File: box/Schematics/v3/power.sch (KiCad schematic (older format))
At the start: 29 parts, among them U1 AMC1100DWV, U3 ISL21010CFH333Z-TK

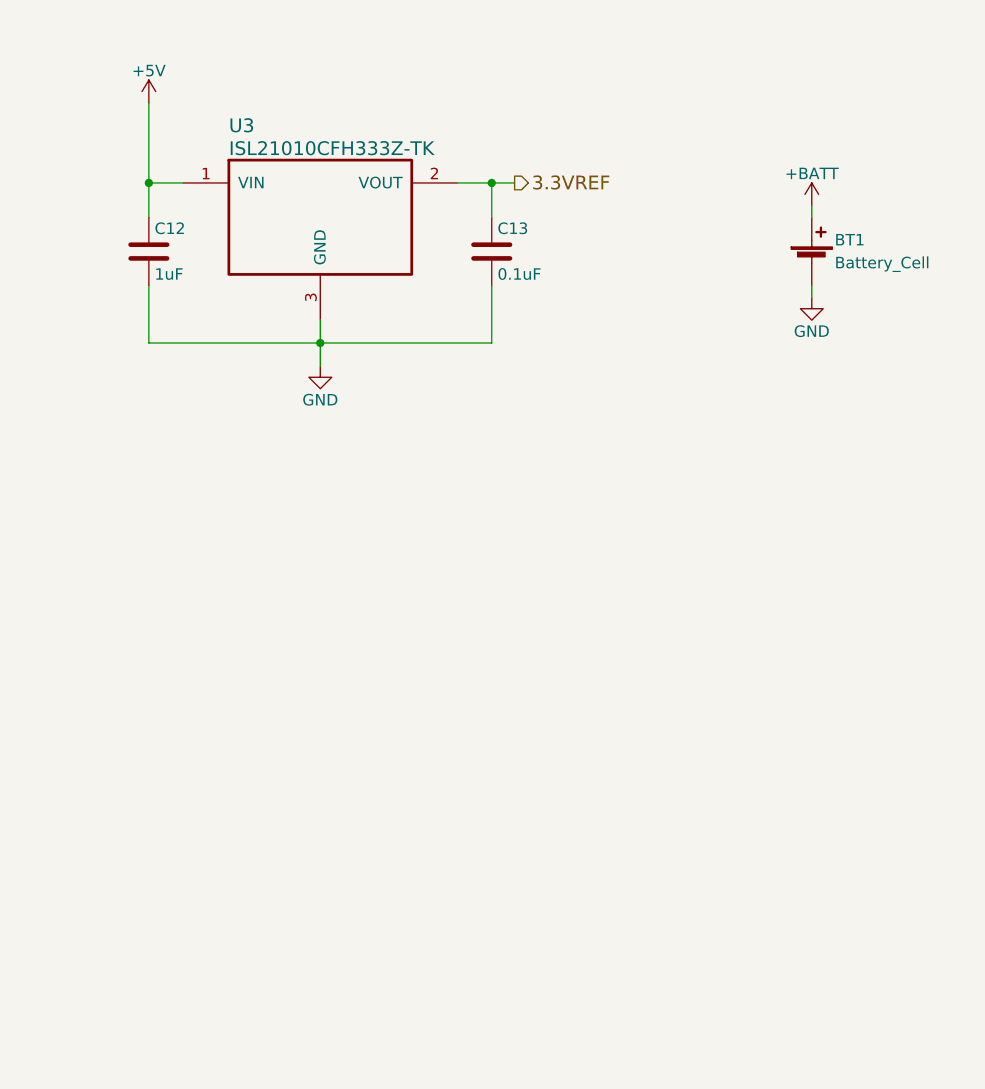
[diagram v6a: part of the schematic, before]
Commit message: remove chip, replace pi
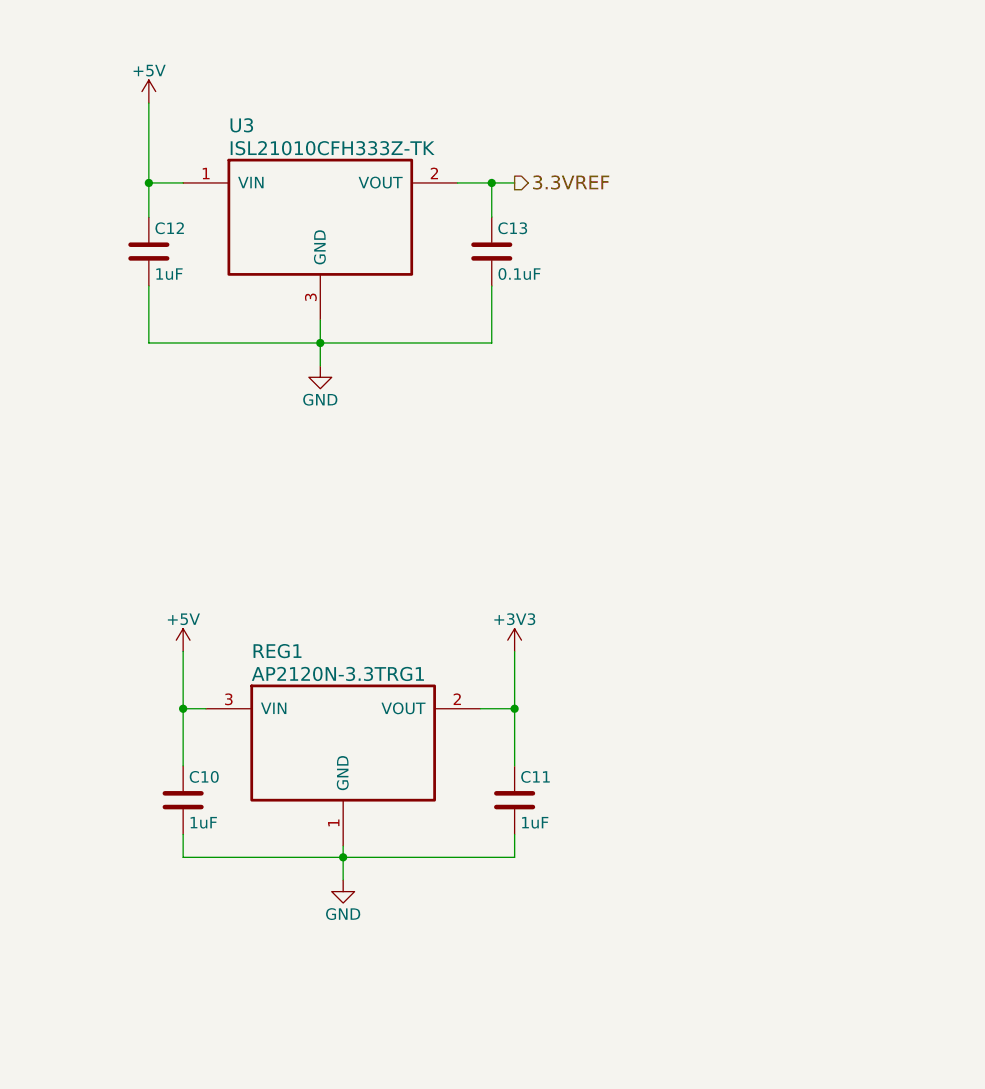
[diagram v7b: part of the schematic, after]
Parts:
- removed BT1: Battery_Cell, Connectors_JST:JST_PH_B2B-PH-K_02x2.00mm_Straight, symbol Battery_Cell
- added C10, C11: 1uF, Capacitors_SMD:C_0603_HandSoldering, symbol C
- added REG1: AP2120N-3.3TRG1, TO_SOT_Packages_SMD:SOT-23, symbol AP2120N-3.3TRG1
- PSU2: footprint (none) -> Housings_SSOP:SSOP-20_5.3x7.2mm_Pitch0.65mm
- R1, R2: footprint Resistors_THT:R_Axial_DIN0204_L3.6mm_D1.6mm_P5.08mm_Horizontal -> Resistors_THT:R_Axial_DIN0309_L9.0mm_D3.2mm_P15.24mm_Horizontal
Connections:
- net +3V3: now also C11.1, REG1.2 (VOUT)
- net +5V: now also C10.1, REG1.3 (VIN)
- net GND: now also C10.2, C11.2, REG1.1 (GND)
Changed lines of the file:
@@
 F 0 "R1" V 2230 3600 50  0000 C CNN
 F 1 "990k" V 2150 3600 50  0000 C CNN
-F 2 "Resistors_THT:R_Axial_DIN0204_L3.6mm_D1.6mm_P5.08mm_Horizontal" V 2080 3600 50  0001 C CNN
+F 2 "Resistors_THT:R_Axial_DIN0309_L9.0mm_D3.2mm_P15.24mm_Horizontal" V 2080 3600 50  0001 C CNN
 F 3 "" H 2150 3600 50  0001 C CNN
 	1    2150 3600
@@
 F 0 "R2" V 2230 4150 50  0000 C CNN
 F 1 "1k" V 2150 4150 50  0000 C CNN
-F 2 "Resistors_THT:R_Axial_DIN0204_L3.6mm_D1.6mm_P5.08mm_Horizontal" V 2080 4150 50  0001 C CNN
+F 2 "Resistors_THT:R_Axial_DIN0309_L9.0mm_D3.2mm_P15.24mm_Horizontal" V 2080 4150 50  0001 C CNN
 F 3 "" H 2150 4150 50  0001 C CNN
 	1    2150 4150
@@
 F 0 "PSU2" H 3250 6450 60  0000 L CNN
 F 1 "ADUM5010ARSZ" H 3250 6350 60  0000 L CNN
-F 2 "" H 3050 6200 60  0001 C CNN
+F 2 "Housings_SSOP:SSOP-20_5.3x7.2mm_Pitch0.65mm" H 3050 6200 60  0001 C CNN
 F 3 "" H 3050 6200 60  0001 C CNN
 	1    3050 6200
@@
 $EndComp
 $Comp
-L +BATT #PWR021
-U 1 1 5A9BB5CB
-P 9600 1600
-F 0 "#PWR021" H 9600 1450 50  0001 C CNN
-F 1 "+BATT" H 9600 1740 50  0000 C CNN
-F 2 "" H 9600 1600 50  0001 C CNN
-F 3 "" H 9600 1600 50  0001 C CNN
-	1    9600 1600
-	1    0    0    -1
-$EndComp
-$Comp
-L Battery_Cell BT1
-U 1 1 5A9BB715
-P 9600 1850
-F 0 "BT1" H 9700 1950 50  0000 L CNN
-F 1 "Battery_Cell" H 9700 1850 50  0000 L CNN
-F 2 "Connectors_JST:JST_PH_B2B-PH-K_02x2.00mm_Straight" V 9600 1910 50  0001 C CNN
-F 3 "" V 9600 1910 50  0001 C CNN
-	1    9600 1850
-	1    0    0    -1
-$EndComp
-$Comp
-L GND #PWR022
-U 1 1 5A9BB982
-P 9600 2000
-F 0 "#PWR022" H 9600 1750 50  0001 C CNN
-F 1 "GND" H 9600 1850 50  0000 C CNN
-F 2 "" H 9600 2000 50  0001 C CNN
-F 3 "" H 9600 2000 50  0001 C CNN
-	1    9600 2000
-	1    0    0    -1
-$EndComp
-Wire Wire Line
-	9600 2000 9600 1950
-Wire Wire Line
-	9600 1600 9600 1650
+L AP2120N-3.3TRG1 REG1
+U 1 1 5AC2DFBA
+P 6950 3800
+F 0 "REG1" H 7150 4050 60  0000 L CNN
+F 1 "AP2120N-3.3TRG1" H 7150 3950 60  0000 L CNN
+F 2 "TO_SOT_Packages_SMD:SOT-23" H 6950 3800 60  0001 C CNN
+F 3 "" H 6950 3800 60  0001 C CNN
+	1    6950 3800
+	1    0    0    -1
+$EndComp
+$Comp
+L C C10
+U 1 1 5AC2E23F
+P 6850 4200
+F 0 "C10" H 6875 4300 50  0000 L CNN
+F 1 "1uF" H 6875 4100 50  0000 L CNN
+F 2 "Capacitors_SMD:C_0603_HandSoldering" H 6888 4050 50  0001 C CNN
+F 3 "" H 6850 4200 50  0001 C CNN
+	1    6850 4200
+	1    0    0    -1
+$EndComp
+$Comp
+L C C11
+U 1 1 5AC2E2AC
+P 8300 4200
+F 0 "C11" H 8325 4300 50  0000 L CNN
+F 1 "1uF" H 8325 4100 50  0000 L CNN
+F 2 "Capacitors_SMD:C_0603_HandSoldering" H 8338 4050 50  0001 C CNN
+F 3 "" H 8300 4200 50  0001 C CNN
+	1    8300 4200
+	1    0    0    -1
+$EndComp
+$Comp
+L GND #PWR021
+U 1 1 5AC2E311
+P 7550 4550
+F 0 "#PWR021" H 7550 4300 50  0001 C CNN
+F 1 "GND" H 7550 4400 50  0000 C CNN
+F 2 "" H 7550 4550 50  0001 C CNN
+F 3 "" H 7550 4550 50  0001 C CNN
+	1    7550 4550
+	1    0    0    -1
+$EndComp
+Wire Wire Line
+	6850 4350 6850 4450
+Wire Wire Line
+	6850 4450 8300 4450
+Wire Wire Line
+	7550 4400 7550 4550
+Connection ~ 7550 4450
+Wire Wire Line
+	8300 4450 8300 4350
+Wire Wire Line
+	6950 3800 6850 3800
+Wire Wire Line
+	6850 3550 6850 4050
+Wire Wire Line
+	8150 3800 8300 3800
+Wire Wire Line
+	8300 3550 8300 4050
+$Comp
+L +3V3 #PWR022
+U 1 1 5AC2E6F2
+P 8300 3550
+F 0 "#PWR022" H 8300 3400 50  0001 C CNN
+F 1 "+3V3" H 8300 3690 50  0000 C CNN
+F 2 "" H 8300 3550 50  0001 C CNN
+F 3 "" H 8300 3550 50  0001 C CNN
+	1    8300 3550
+	1    0    0    -1
+$EndComp
+$Comp
+L +5V #PWR023
+U 1 1 5AC2E744
+P 6850 3550
+F 0 "#PWR023" H 6850 3400 50  0001 C CNN
+F 1 "+5V" H 6850 3690 50  0000 C CNN
+F 2 "" H 6850 3550 50  0001 C CNN
+F 3 "" H 6850 3550 50  0001 C CNN
+	1    6850 3550
+	1    0    0    -1
+$EndComp
+Connection ~ 6850 3800
+Connection ~ 8300 3800
 $EndSCHEMATC

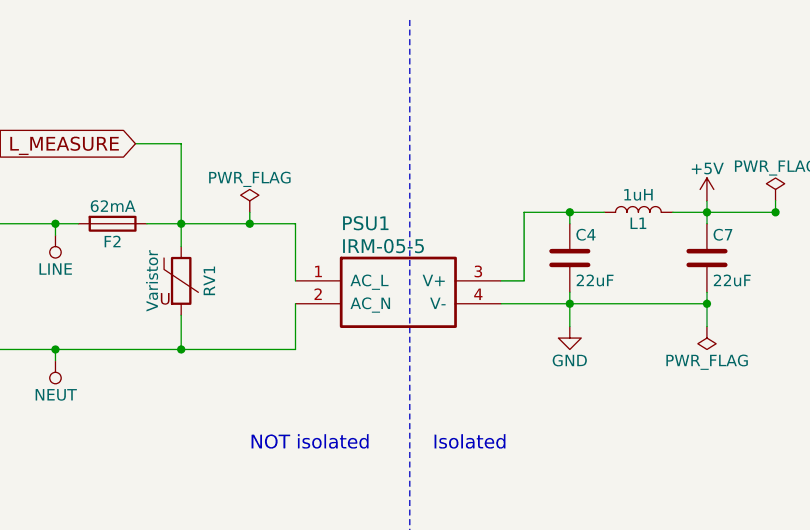
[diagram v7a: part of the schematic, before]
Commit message: add IRM-15-05 and replace 05
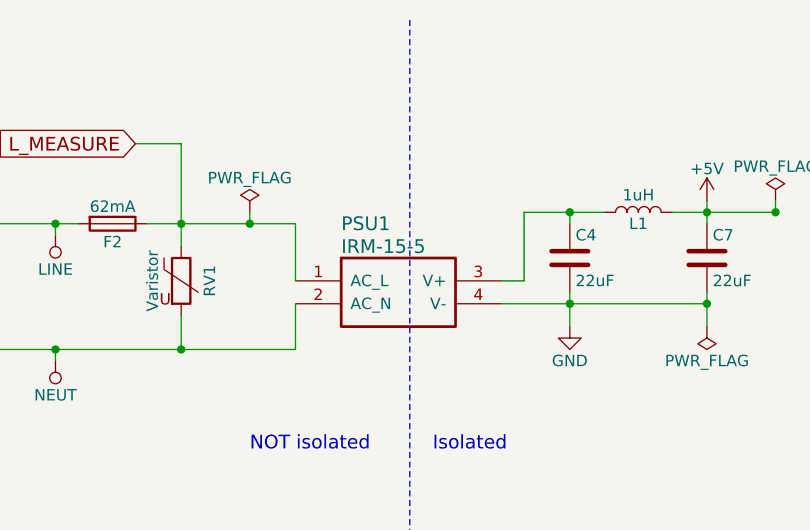
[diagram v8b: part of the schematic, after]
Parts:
- removed PSU1: IRM-05-5, opqbox3:IRM-05-5, symbol IRM-05-5
- added PSU1: IRM-15-5, symbol IRM-15-5
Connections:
- net GND: now also PSU1.4 (V-)
- net L_MEASURE: now also PSU1.1 (AC_L)
- net NEUT: now also PSU1.2 (AC_N)
- net at C4.1, L1.1: now also PSU1.3 (V+)
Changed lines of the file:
@@
 $EndComp
 $Comp
-L IRM-05-5 PSU1
-U 1 1 5A829FB6
-P 3100 1650
-F 0 "PSU1" H 3300 1900 60  0000 L CNN
-F 1 "IRM-05-5" H 3300 1800 60  0000 L CNN
-F 2 "opqbox3:IRM-05-5" H 3100 1650 60  0001 C CNN
-F 3 "" H 3100 1650 60  0001 C CNN
-	1    3100 1650
-	1    0    0    -1
-$EndComp
-$Comp
-L GND #PWR03
+L GND #PWR7
 U 1 1 5A829FB7
 P 4300 1850
-F 0 "#PWR03" H 4300 1600 50  0001 C CNN
+F 0 "#PWR7" H 4300 1600 50  0001 C CNN
 F 1 "GND" H 4300 1700 50  0000 C CNN
 F 2 "" H 4300 1850 50  0001 C CNN
@@
 $EndComp
 $Comp
-L +5V #PWR04
+L +5V #PWR13
 U 1 1 5A829FBB
 P 4900 1300
-F 0 "#PWR04" H 4900 1150 50  0001 C CNN
+F 0 "#PWR13" H 4900 1150 50  0001 C CNN
 F 1 "+5V" H 4900 1440 50  0000 C CNN
 F 2 "" H 4900 1300 50  0001 C CNN
@@
 L_MEASURE
 $Comp
-L NEUT #PWR05
+L NEUT #PWR2
 U 1 1 5A829FBC
 P 2050 2000
-F 0 "#PWR05" H 2050 1850 50  0001 C CNN
+F 0 "#PWR2" H 2050 1850 50  0001 C CNN
 F 1 "NEUT" H 2050 2150 50  0000 C CNN
 F 2 "" H 2050 2000 50  0001 C CNN
@@
 $EndComp
 $Comp
-L LINE #PWR06
+L LINE #PWR1
 U 1 1 5A829FBD
 P 2050 1450
-F 0 "#PWR06" H 2050 1300 50  0001 C CNN
+F 0 "#PWR1" H 2050 1300 50  0001 C CNN
 F 1 "LINE" H 2050 1600 50  0000 C CNN
 F 2 "" H 2050 1450 50  0001 C CNN
@@
 $EndComp
 $Comp
-L PWR_FLAG #FLG07
+L PWR_FLAG #FLG3
 U 1 1 5A829FC1
 P 2900 1350
-F 0 "#FLG07" H 2900 1425 50  0001 C CNN
+F 0 "#FLG3" H 2900 1425 50  0001 C CNN
 F 1 "PWR_FLAG" H 2900 1500 50  0000 C CNN
 F 2 "" H 2900 1350 50  0001 C CNN
@@
 $EndComp
 $Comp
-L PWR_FLAG #FLG08
+L PWR_FLAG #FLG5
 U 1 1 5A829FC2
 P 5200 1300
-F 0 "#FLG08" H 5200 1375 50  0001 C CNN
+F 0 "#FLG5" H 5200 1375 50  0001 C CNN
 F 1 "PWR_FLAG" H 5200 1450 50  0000 C CNN
 F 2 "" H 5200 1300 50  0001 C CNN
@@
 $EndComp
 $Comp
-L NEUT #PWR09
+L NEUT #PWR5
 U 1 1 5A829FC9
 P 2650 4700
-F 0 "#PWR09" H 2650 4550 50  0001 C CNN
+F 0 "#PWR5" H 2650 4550 50  0001 C CNN
 F 1 "NEUT" H 2650 4850 50  0000 C CNN
 F 2 "" H 2650 4700 50  0001 C CNN
@@
 $EndComp
 $Comp
-L NEUT #PWR010
+L NEUT #PWR4
 U 1 1 5A829FCE
 P 2650 3600
-F 0 "#PWR010" H 2650 3450 50  0001 C CNN
+F 0 "#PWR4" H 2650 3450 50  0001 C CNN
 F 1 "NEUT" H 2650 3750 50  0000 C CNN
 F 2 "" H 2650 3600 50  0001 C CNN
@@
 $EndComp
 $Comp
-L NEUT #PWR011
+L NEUT #PWR6
 U 1 1 5A829FD1
 P 3050 5850
-F 0 "#PWR011" H 3050 5700 50  0001 C CNN
+F 0 "#PWR6" H 3050 5700 50  0001 C CNN
 F 1 "NEUT" H 3050 6000 50  0000 C CNN
 F 2 "" H 3050 5850 50  0001 C CNN
@@
 $EndComp
 $Comp
-L NEUT #PWR012
+L NEUT #PWR3
 U 1 1 5A829FD4
 P 2400 6850
-F 0 "#PWR012" H 2400 6700 50  0001 C CNN
+F 0 "#PWR3" H 2400 6700 50  0001 C CNN
 F 1 "NEUT" H 2400 7000 50  0000 C CNN
 F 2 "" H 2400 6850 50  0001 C CNN
@@
 NOT isolated
 $Comp
-L GND #PWR013
+L GND #PWR11
 U 1 1 5A829FD5
 P 4450 6850
-F 0 "#PWR013" H 4450 6600 50  0001 C CNN
+F 0 "#PWR11" H 4450 6600 50  0001 C CNN
 F 1 "GND" H 4450 6700 50  0000 C CNN
 F 2 "" H 4450 6850 50  0001 C CNN
@@
 $EndComp
 $Comp
-L +5V #PWR014
+L +5V #PWR10
 U 1 1 5A829FD7
 P 4450 5700
-F 0 "#PWR014" H 4450 5550 50  0001 C CNN
+F 0 "#PWR10" H 4450 5550 50  0001 C CNN
 F 1 "+5V" H 4450 5840 50  0000 C CNN
 F 2 "" H 4450 5700 50  0001 C CNN
@@
 $EndComp
 $Comp
-L GND #PWR015
+L GND #PWR8
 U 1 1 5A829FDA
 P 4350 4300
-F 0 "#PWR015" H 4350 4050 50  0001 C CNN
+F 0 "#PWR8" H 4350 4050 50  0001 C CNN
 F 1 "GND" H 4350 4150 50  0000 C CNN
 F 2 "" H 4350 4300 50  0001 C CNN
@@
 $EndComp
 $Comp
-L +3.3V #PWR016
+L +3.3V #PWR12
 U 1 1 5A829FDB
 P 4650 3150
-F 0 "#PWR016" H 4650 3000 50  0001 C CNN
+F 0 "#PWR12" H 4650 3000 50  0001 C CNN
 F 1 "+3.3V" H 4650 3290 50  0000 C CNN
 F 2 "" H 4650 3150 50  0001 C CNN
@@
 $EndComp
 $Comp
-L GND #PWR017
+L GND #PWR9
 U 1 1 5A829FE0
 P 4400 3600
-F 0 "#PWR017" H 4400 3350 50  0001 C CNN
+F 0 "#PWR9" H 4400 3350 50  0001 C CNN
 F 1 "GND" H 4400 3450 50  0000 C CNN
 F 2 "" H 4400 3600 50  0001 C CNN
@@
 NEUTRAL
 $Comp
-L PWR_FLAG #FLG018
+L PWR_FLAG #FLG4
 U 1 1 5A83249D
 P 4900 1850
-F 0 "#FLG018" H 4900 1925 50  0001 C CNN
+F 0 "#FLG4" H 4900 1925 50  0001 C CNN
 F 1 "PWR_FLAG" H 4900 2000 50  0000 C CNN
 F 2 "" H 4900 1850 50  0001 C CNN
@@
 $EndComp
 $Comp
-L +5V #PWR019
+L +5V #PWR14
 U 1 1 5A82BC82
 P 6700 1150
-F 0 "#PWR019" H 6700 1000 50  0001 C CNN
+F 0 "#PWR14" H 6700 1000 50  0001 C CNN
 F 1 "+5V" H 6700 1290 50  0000 C CNN
 F 2 "" H 6700 1150 50  0001 C CNN
@@
 Connection ~ 8200 1500
 $Comp
-L GND #PWR020
+L GND #PWR16
 U 1 1 5A82C977
 P 7450 2300
-F 0 "#PWR020" H 7450 2050 50  0001 C CNN
+F 0 "#PWR16" H 7450 2050 50  0001 C CNN
 F 1 "GND" H 7450 2150 50  0000 C CNN
 F 2 "" H 7450 2300 50  0001 C CNN
@@
 $EndComp
 $Comp
-L GND #PWR021
+L GND #PWR17
 U 1 1 5AC2E311
 P 7550 4550
-F 0 "#PWR021" H 7550 4300 50  0001 C CNN
+F 0 "#PWR17" H 7550 4300 50  0001 C CNN
 F 1 "GND" H 7550 4400 50  0000 C CNN
 F 2 "" H 7550 4550 50  0001 C CNN
@@
 	8300 3550 8300 4050
 $Comp
-L +3V3 #PWR022
+L +3V3 #PWR18
 U 1 1 5AC2E6F2
 P 8300 3550
-F 0 "#PWR022" H 8300 3400 50  0001 C CNN
+F 0 "#PWR18" H 8300 3400 50  0001 C CNN
 F 1 "+3V3" H 8300 3690 50  0000 C CNN
 F 2 "" H 8300 3550 50  0001 C CNN
@@
 $EndComp
 $Comp
-L +5V #PWR023
+L +5V #PWR15
 U 1 1 5AC2E744
 P 6850 3550
-F 0 "#PWR023" H 6850 3400 50  0001 C CNN
+F 0 "#PWR15" H 6850 3400 50  0001 C CNN
 F 1 "+5V" H 6850 3690 50  0000 C CNN
 F 2 "" H 6850 3550 50  0001 C CNN
@@
 Connection ~ 6850 3800
 Connection ~ 8300 3800
+$Comp
+L IRM-15-5 PSU1
+U 1 1 5ACB4D59
+P 3100 1650
+F 0 "PSU1" H 3300 1900 60  0000 L CNN
+F 1 "IRM-15-5" H 3300 1800 60  0000 L CNN
+F 2 "" H 3100 1650 60  0001 C CNN
+F 3 "" H 3100 1650 60  0001 C CNN
+	1    3100 1650
+	1    0    0    -1
+$EndComp
 $EndSCHEMATC
